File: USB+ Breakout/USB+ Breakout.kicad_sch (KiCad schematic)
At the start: 6 parts, among them J101 Conn_01x10, J301 Conn_01x10

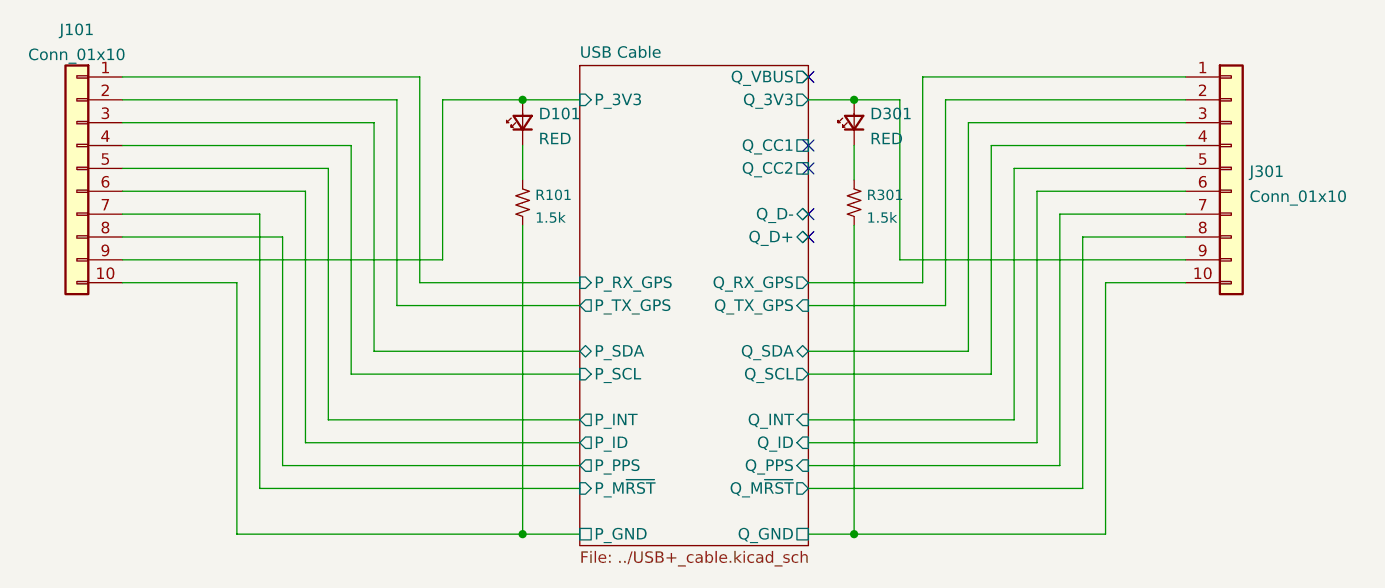
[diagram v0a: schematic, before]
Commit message: Updated LEDs and edge cutouts
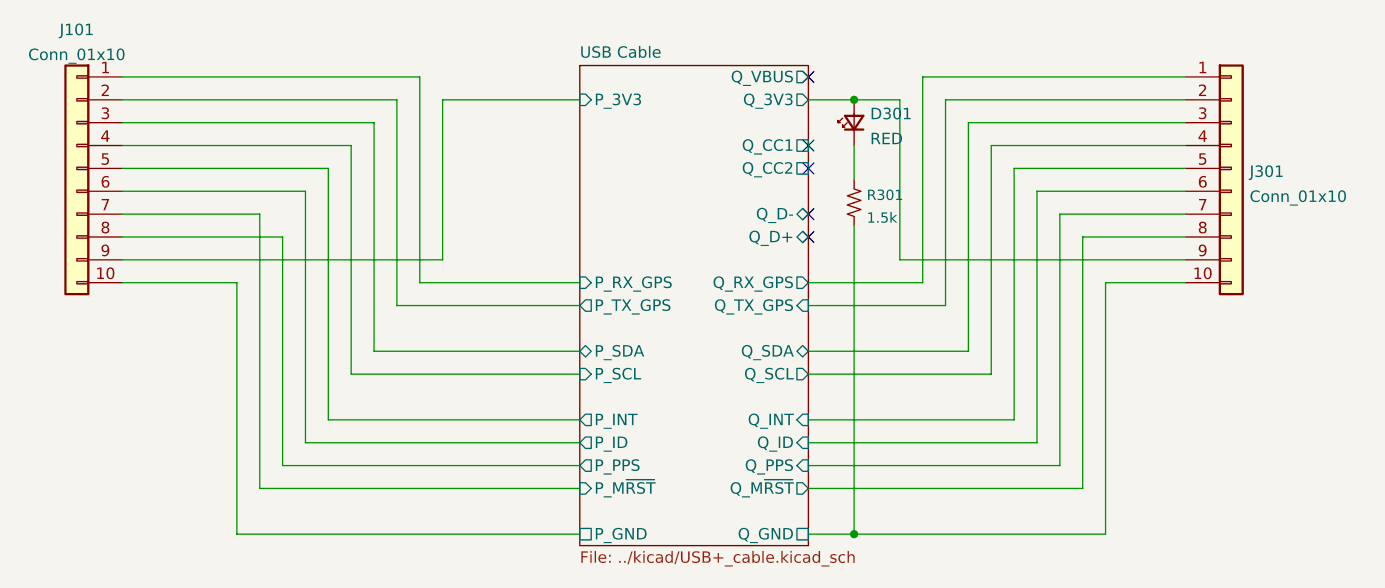
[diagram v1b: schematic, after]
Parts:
- removed D101: RED, LED_SMD:LED_0603_1608Metric, symbol Device:LED_Small
- removed R101: 1.5k, Resistor_SMD:R_0603_1608Metric, symbol KwanSystems:RESISTOR
- R301: footprint Resistor_SMD:R_0603_1608Metric -> Resistor_SMD:R_0402_1005Metric
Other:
- sheet USB Cable: file ../USB+_cable.kicad_sch -> ../kicad/USB+_cable.kicad_sch
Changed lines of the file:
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@@
   (junction (at 119.38 101.6) (diameter 0) (color 0 0 0 0)
   )
-  (junction (at 82.55 101.6) (diameter 0) (color 0 0 0 0)
-  )
   (junction (at 119.38 53.34) (diameter 0) (color 0 0 0 0)
-  )
-  (junction (at 82.55 53.34) (diameter 0) (color 0 0 0 0)
   )
   (no_connect (at 114.3 66.04))
@@
     (stroke (width 0) (type default) (color 0 0 0 0))
   )
-  (wire (pts (xy 82.55 101.6) (xy 50.8 101.6))
+  (wire (pts (xy 50.8 101.6) (xy 88.9 101.6))
     (stroke (width 0) (type default) (color 0 0 0 0))
   )
@@
     (stroke (width 0) (type default) (color 0 0 0 0))
   )
-  (wire (pts (xy 82.55 58.42) (xy 82.55 62.23))
-    (stroke (width 0) (type default) (color 0 0 0 0))
-  )
-  (wire (pts (xy 82.55 53.34) (xy 88.9 53.34))
-    (stroke (width 0) (type default) (color 0 0 0 0))
-  )
   (wire (pts (xy 88.9 93.98) (xy 55.88 93.98))
     (stroke (width 0) (type default) (color 0 0 0 0))
@@
     (stroke (width 0) (type default) (color 0 0 0 0))
   )
-  (wire (pts (xy 73.66 53.34) (xy 82.55 53.34))
+  (wire (pts (xy 73.66 53.34) (xy 88.9 53.34))
     (stroke (width 0) (type default) (color 0 0 0 0))
   )
@@
   )
   (wire (pts (xy 55.88 68.58) (xy 55.88 93.98))
-    (stroke (width 0) (type default) (color 0 0 0 0))
-  )
-  (wire (pts (xy 82.55 67.31) (xy 82.55 101.6))
-    (stroke (width 0) (type default) (color 0 0 0 0))
-  )
-  (wire (pts (xy 88.9 101.6) (xy 82.55 101.6))
     (stroke (width 0) (type default) (color 0 0 0 0))
   )
@@
       (effects (font (size 1.143 1.143)) (justify right))
     )
-    (property "Footprint" "Resistor_SMD:R_0603_1608Metric" (id 2) (at 115.57 63.373 0)
+    (property "Footprint" "Resistor_SMD:R_0402_1005Metric" (id 2) (at 115.57 63.373 0)
       (effects (font (size 0.508 0.508)) hide)
     )
@@
     (pin "9")
   )
-  (symbol (lib_id "Device:LED_Small") (at 82.55 55.88 90) (unit 1)
-    (in_bom yes) (on_board yes) (fields_autoplaced)
-    (property "Reference" "D101" (id 0) (at 84.328 54.908 90)
-      (effects (font (size 1.27 1.27)) (justify right))
-    )
-    (property "Value" "RED" (id 1) (at 84.328 57.6831 90)
-      (effects (font (size 1.27 1.27)) (justify right))
-    )
-    (property "Footprint" "LED_SMD:LED_0603_1608Metric" (id 2) (at 82.55 55.88 90)
-      (effects (font (size 1.27 1.27)) hide)
-    )
-    (property "Datasheet" "~" (id 3) (at 82.55 55.88 90)
-      (effects (font (size 1.27 1.27)) hide)
-    )
-    (pin "1")
-    (pin "2")
-  )
-  (symbol (lib_id "KwanSystems:RESISTOR") (at 82.55 64.77 90) (unit 1)
-    (in_bom yes) (on_board yes) (fields_autoplaced)
-    (property "Reference" "R101" (id 0) (at 83.947 63.9397 90)
-      (effects (font (size 1.143 1.143)) (justify right))
-    )
-    (property "Value" "1.5k" (id 1) (at 83.947 66.4625 90)
-      (effects (font (size 1.143 1.143)) (justify right))
-    )
-    (property "Footprint" "Resistor_SMD:R_0603_1608Metric" (id 2) (at 78.74 63.373 0)
-      (effects (font (size 0.508 0.508)) hide)
-    )
-    (property "Datasheet" "" (id 3) (at 90.17 53.975 0)
-      (effects (font (size 1.524 1.524)) hide)
-    )
-    (pin "1")
-    (pin "2")
-  )
   (symbol (lib_id "Connector_Generic:Conn_01x10") (at 161.29 60.96 0) (unit 1)
     (in_bom yes) (on_board yes) (fields_autoplaced)
@@
       (effects (font (size 1.27 1.27)) (justify left bottom))
     )
-    (property "Sheet file" "../USB+_cable.kicad_sch" (id 1) (at 88.9 103.4546 0)
+    (property "Sheet file" "../kicad/USB+_cable.kicad_sch" (id 1) (at 88.9 103.4546 0)
       (effects (font (size 1.27 1.27)) (justify left top))
     )
@@
   )
   (symbol_instances
-    (path "/7e3c6e1c-7b06-437c-ab81-45577829a98e"
-      (reference "D101") (unit 1) (value "RED") (footprint "LED_SMD:LED_0603_1608Metric")
-    )
     (path "/f29d7664-ef88-4da2-9ab0-637d5046eaf9"
       (reference "D301") (unit 1) (value "RED") (footprint "LED_SMD:LED_0603_1608Metric")
     )
+    (path "/4ec618ae-096f-4256-9328-005ee04f13d6/250dc1a6-364c-43f2-aa95-90d20389c1bd"
+      (reference "D1601") (unit 1) (value "GREEN, YELLOW") (footprint "KwanSystems:LEDKingbrightAPHB")
+    )
     (path "/36280559-4de9-47fb-843f-86081cd88eac"
       (reference "J101") (unit 1) (value "Conn_01x10") (footprint "Connector_PinHeader_2.54mm:PinHeader_1x10_P2.54mm_Vertical")
     )
-    (path "/4ec618ae-096f-4256-9328-005ee04f13d6/088528ed-9597-4a2f-884e-b077d4d99f3c"
-      (reference "J201") (unit 1) (value "USB_C_Receptacle") (footprint "KwanSystems:USB_C_Amphenol_MidMount")
-    )
-    (path "/4ec618ae-096f-4256-9328-005ee04f13d6/a28887cd-2bdd-4ab6-b51e-99cd821ad1c9"
-      (reference "J202") (unit 1) (value "USB_C_Receptacle") (footprint "KwanSystems:USB_C_Amphenol_MidMount")
-    )
     (path "/e4deb2aa-5602-4d24-baee-8301e95df3c1"
       (reference "J301") (unit 1) (value "Conn_01x10") (footprint "Connector_PinHeader_2.54mm:PinHeader_1x10_P2.54mm_Vertical")
     )
-    (path "/819c0efd-4a61-4f31-a598-087534775904"
-      (reference "R101") (unit 1) (value "1.5k") (footprint "Resistor_SMD:R_0603_1608Metric")
+    (path "/4ec618ae-096f-4256-9328-005ee04f13d6/088528ed-9597-4a2f-884e-b077d4d99f3c"
+      (reference "J1601") (unit 1) (value "USB_C_Receptacle") (footprint "KwanSystems:USB_C_Amphenol_MidMount")
+    )
+    (path "/4ec618ae-096f-4256-9328-005ee04f13d6/a28887cd-2bdd-4ab6-b51e-99cd821ad1c9"
+      (reference "J1602") (unit 1) (value "USB_C_Receptacle") (footprint "KwanSystems:USB_C_Amphenol_MidMount")
     )
     (path "/323b7586-1642-40cf-b5d6-43954976ee91"
-      (reference "R301") (unit 1) (value "1.5k") (footprint "Resistor_SMD:R_0603_1608Metric")
-    )
-  )
+      (reference "R301") (unit 1) (value "1.5k") (footprint "Resistor_SMD:R_0402_1005Metric")
+    )
+    (path "/4ec618ae-096f-4256-9328-005ee04f13d6/54433dd4-adee-4336-973f-b7d943e3b941"
+      (reference "R1601") (unit 1) (value "330") (footprint "Resistor_SMD:R_0402_1005Metric")
+    )
+    (path "/4ec618ae-096f-4256-9328-005ee04f13d6/e199ed72-6b3b-4ec7-a4ea-7a28131416d7"
+      (reference "R1602") (unit 1) (value "1.5k") (footprint "Resistor_SMD:R_0402_1005Metric")
+    )
+  )
